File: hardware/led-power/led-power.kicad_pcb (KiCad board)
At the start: 4 copper layers, 86.4 x 86.4 mm, 104 parts, among them J1 String1, J10 PowerInput, J11 Qwiic, J12 Qwiic, J13 A0, J14 A1, J15 A2, J16 I2C Header, J17 IRQ, J2 String2, J3 String3, J4 String4, J5 String5, J6 String6, J7 String7, J8 String8, J9 PowerInput, Q1 Q_NMOS_GDS, Q2 Q_NMOS_GDS, Q3 Q_NMOS_GDS, Q4 Q_NMOS_GDS, Q5 Q_NMOS_GDS, Q6 Q_NMOS_GDS, Q7 Q_NMOS_GDS, Q8 Q_NMOS_GDS, U1 MCP6V51, U10 L78L05ACZ-AP, U11 MCP1501, U2 MCP6V51, U3 MCP6V51, U4 MCP6V51, U5 MCP6V51, U6 MCP6V51, U7 MCP6V51, U8 MCP6V51, U9 MCP23017_SO

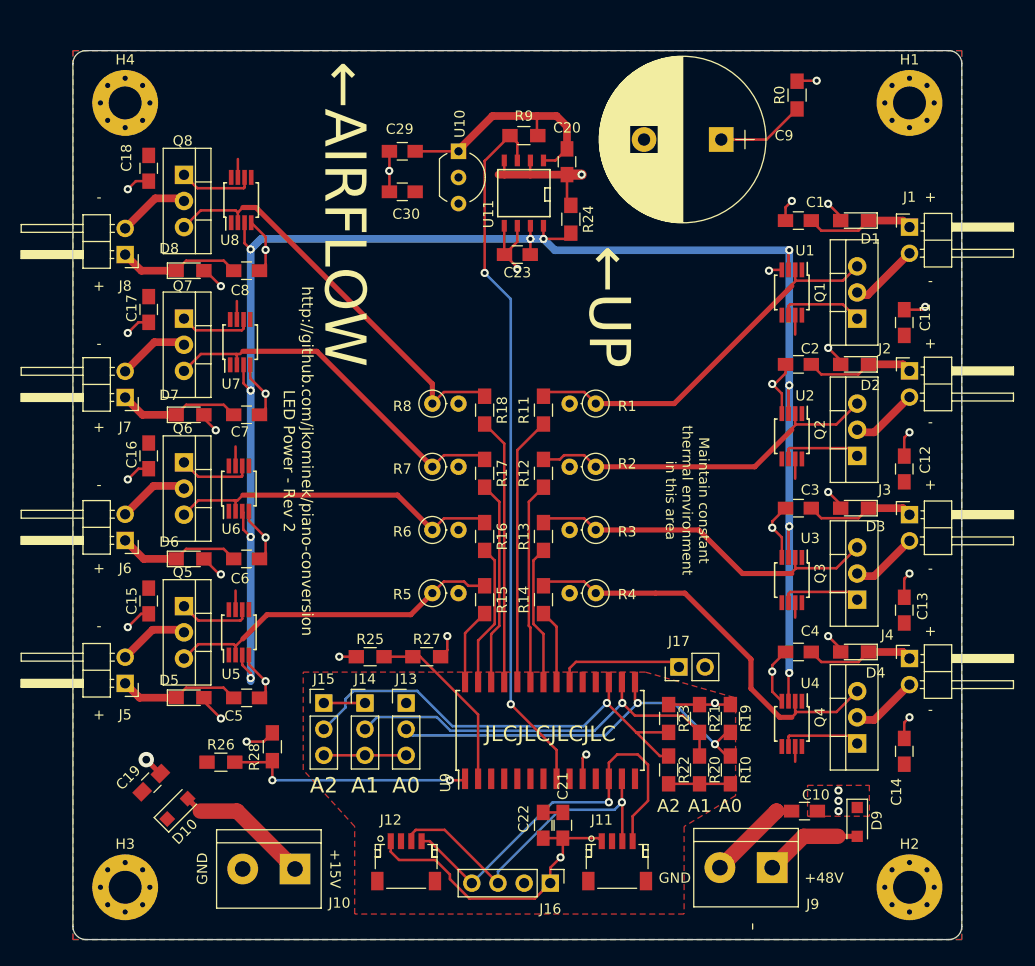
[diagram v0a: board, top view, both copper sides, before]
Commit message: LED power board improvements, per issue #42
* Increased thermal relief
* Moved C10 well away from J9
* R24 and R9 are now the same value, 3.6kohm
* Removed R0
* Removed the need for the +15V supply with an LM317.
* Removed I2C IO expander and replaced with an STM32G0
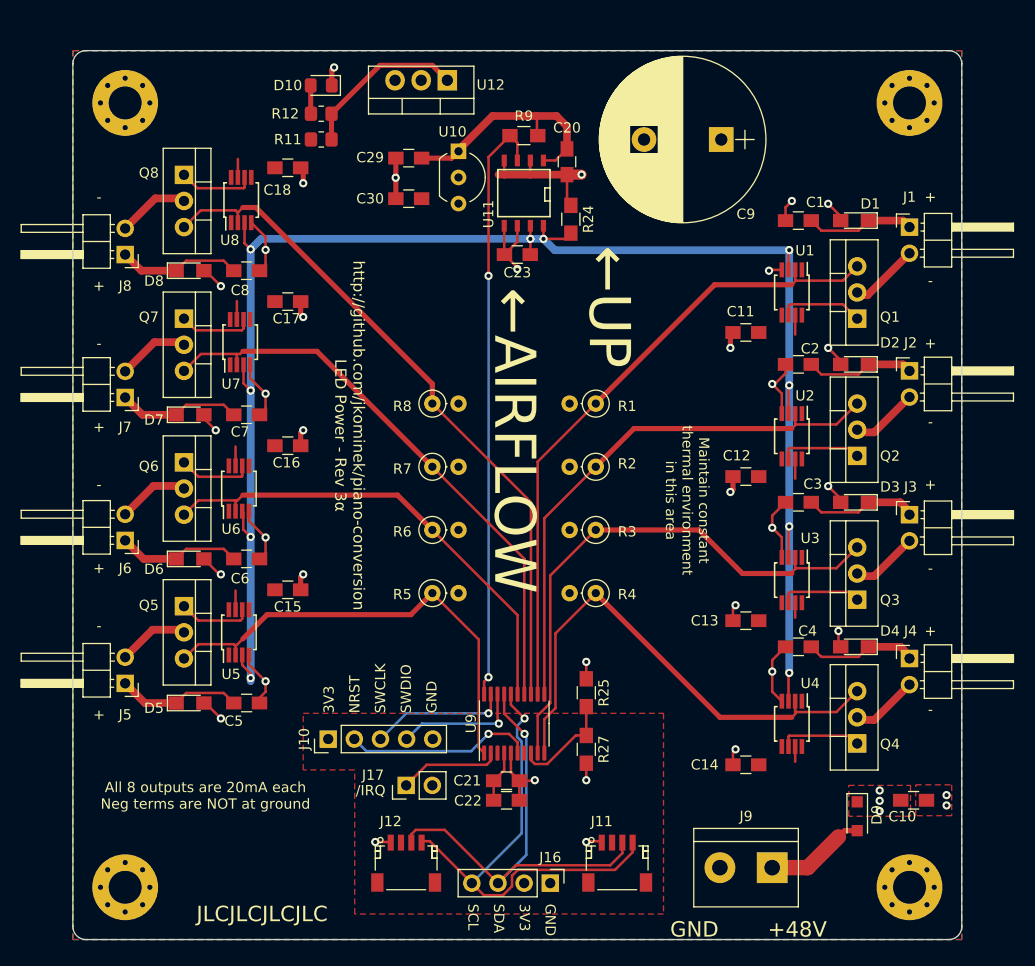
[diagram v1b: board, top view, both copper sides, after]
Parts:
- removed C19: .1uF, Capacitors_SMD:C_0805_HandSoldering
- removed J13: A0, Pin_Headers:Pin_Header_Straight_1x03_Pitch2.54mm
- removed J14: A1, Pin_Headers:Pin_Header_Straight_1x03_Pitch2.54mm
- removed J15: A2, Pin_Headers:Pin_Header_Straight_1x03_Pitch2.54mm
- removed R0: Dissipate, Resistors_SMD:R_0805_HandSoldering
- removed R10, R19, R20, R21, R22, R23: DNP, Resistors_SMD:R_0805_HandSoldering
- removed R13, R14, R15, R16, R17, R18: 43k, Resistors_SMD:R_0805_HandSoldering
- removed R26: 1300, Resistors_SMD:R_0805_HandSoldering
- removed R28: 330, Resistors_SMD:R_0805_HandSoldering
- added U12: LM317_TO-220, Package_TO_SOT_THT:TO-220-3_Vertical, F.Cu at (107.5, 74.0)
- D10: value D_Small_ALT -> 2.2Vf; footprint Diodes_SMD:D_SOD-123F -> LED_SMD:LED_0805_2012Metric_Pad1.15x1.40mm_HandSolder
- J10: value PowerInput -> Conn_01x05_Male; footprint Connectors_Terminal_Blocks:TerminalBlock_bornier-2_P5.08mm -> Connector_PinHeader_2.54mm:PinHeader_1x05_P2.54mm_Vertical
- R11: value 43k -> 1000; footprint Resistors_SMD:R_0805_HandSoldering -> Resistor_SMD:R_0805_2012Metric_Pad1.20x1.40mm_HandSolder
- R12: value 43k -> 6800; footprint Resistors_SMD:R_0805_HandSoldering -> Resistor_SMD:R_0805_2012Metric_Pad1.20x1.40mm_HandSolder
- R25: value 4700 -> 110k
- R27: value 330 -> 8.2k
- U9: value MCP23017_SO -> STM32G030Fx; footprint Housings_SOIC:SOIC-28W_7.5x17.9mm_Pitch1.27mm -> Package_SO:TSSOP-20_4.4x6.5mm_P0.65mm
- moved D10 71.7 mm to (95.2, 74.5), turned to 180 degrees
- moved R12 41.1 mm to (95.2, 77.2), turned to 180 degrees
- moved R11 34.0 mm to (95.2, 79.8), turned to 0 degrees
- moved J17 28.9 mm to (103.5, 142.5)
- moved R25 21.3 mm to (121.0, 133.5), turned to -90 degrees
- moved R27 17.9 mm to (121.0, 139.0), turned to -90 degrees
- moved C14 15.4 mm to (136.5, 140.5), turned to 180 degrees
- moved C13 15.4 mm to (136.5, 126.5), turned to 180 degrees
- moved C11 15.4 mm to (136.5, 98.5), turned to 180 degrees
- moved C12 15.4 mm to (136.5, 112.5), turned to 180 degrees
- moved C15 13.6 mm to (92.0, 123.5), turned to 0 degrees
- moved C16 13.6 mm to (92.0, 109.5), turned to 0 degrees
- moved C17 13.5 mm to (92.0, 95.5), turned to 0 degrees
- moved C18 13.5 mm to (92.0, 82.5), turned to 0 degrees
- moved J10 13.0 mm to (95.9, 138.0), turned to 90 degrees
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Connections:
- C11 pad 1: +15V -> +12V
- C12 pad 1: +15V -> +12V
- C13 pad 1: +15V -> +12V
- C14 pad 1: +15V -> +12V
- C15 pad 1: +15V -> +12V
- C16 pad 1: +15V -> +12V
- C17 pad 1: +15V -> +12V
- C18 pad 1: +15V -> +12V
- C30 pad 1: +15V -> +12V
- D10 pad 1: +15V -> GND
- J10 pad 1: Net-(D10-Pad2) -> +3V3
- J10 pad 2: GND -> /NRST
- J17 pad 1: /~IRQ -> /~{IRQ}
- R11 pad 1: /Feedback1 -> +12V
- R12 pad 1: /Feedback2 -> Net-(R11-Pad2)
- R12 pad 2: Net-(R12-Pad2) -> Net-(D10-Pad2)
- R9 pad 2: /~SHDN -> /~{SHDN}
- U1 pad 1: (no net) -> unconnected-(U1-Pad1)
- U1 pad 5: (no net) -> unconnected-(U1-Pad5)
- U1 pad 7: +15V -> +12V
- U1 pad 8: (no net) -> unconnected-(U1-Pad8)
- U10 pad 3: +15V -> +12V
- U11 pad 3: /~SHDN -> /~{SHDN}
- U2 pad 1: (no net) -> unconnected-(U2-Pad1)
- U2 pad 5: (no net) -> unconnected-(U2-Pad5)
- U2 pad 7: +15V -> +12V
- U2 pad 8: (no net) -> unconnected-(U2-Pad8)
- U3 pad 1: (no net) -> unconnected-(U3-Pad1)
- U3 pad 5: (no net) -> unconnected-(U3-Pad5)
- U3 pad 7: +15V -> +12V
- U3 pad 8: (no net) -> unconnected-(U3-Pad8)
- U4 pad 1: (no net) -> unconnected-(U4-Pad1)
- U4 pad 5: (no net) -> unconnected-(U4-Pad5)
- U4 pad 7: +15V -> +12V
- U4 pad 8: (no net) -> unconnected-(U4-Pad8)
- U5 pad 1: (no net) -> unconnected-(U5-Pad1)
- U5 pad 5: (no net) -> unconnected-(U5-Pad5)
- U5 pad 7: +15V -> +12V
- U5 pad 8: (no net) -> unconnected-(U5-Pad8)
- U6 pad 1: (no net) -> unconnected-(U6-Pad1)
- U6 pad 5: (no net) -> unconnected-(U6-Pad5)
- U6 pad 7: +15V -> +12V
- U6 pad 8: (no net) -> unconnected-(U6-Pad8)
- U7 pad 1: (no net) -> unconnected-(U7-Pad1)
- U7 pad 5: (no net) -> unconnected-(U7-Pad5)
- U7 pad 7: +15V -> +12V
- U7 pad 8: (no net) -> unconnected-(U7-Pad8)
- U8 pad 1: (no net) -> unconnected-(U8-Pad1)
- U8 pad 5: (no net) -> unconnected-(U8-Pad5)
- U8 pad 7: +15V -> +12V
- U8 pad 8: (no net) -> unconnected-(U8-Pad8)
- U9 pad 1: /15V_SENSE -> /Feedback5
- U9 pad 10: GND -> /Feedback4
- U9 pad 11: (no net) -> /Feedback2
- U9 pad 12: /SCL -> /Feedback1
- U9 pad 13: /SDA -> /Feedback8
- U9 pad 14: (no net) -> /Feedback7
- U9 pad 15: /A0 -> /Feedback6
- U9 pad 16: /A1 -> /SCL
- U9 pad 17: /A2 -> /SDA
- U9 pad 18: +3V3 -> /SWDIO
- U9 pad 19: (no net) -> /SWCLK
- U9 pad 2: /48V_SENSE -> /~{IRQ}
- U9 pad 20: /~IRQ -> /~{SHDN}
- U9 pad 3: (no net) -> unconnected-(U9-Pad3)
- U9 pad 4: (no net) -> +3V3
- U9 pad 5: (no net) -> GND
- U9 pad 6: (no net) -> /NRST
- U9 pad 7: (no net) -> unconnected-(U9-Pad7)
- U9 pad 8: /~SHDN -> /48V_SENSE
- U9 pad 9: +3V3 -> /Feedback3
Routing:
- net /~SHDN: track 69.1 -> 0.00 mm, vias 2 -> 0
- net /~{SHDN}: track 0.00 -> 58.0 mm, vias 0 -> 2
- net GND: track 148.6 -> 95.4 mm
- net /A2: track 45.3 -> 0.00 mm, vias 1 -> 0
- net /A1: track 40.2 -> 0.00 mm, vias 1 -> 0
- net /A0: track 39.9 -> 0.00 mm, vias 2 -> 0
- net /Feedback8: track 41.1 -> 67.5 mm
- net Net-(R18-Pad2): track 25.9 -> 0.00 mm
- net /Feedback1: track 37.8 -> 62.6 mm
- net /15V_SENSE: track 24.4 -> 0.00 mm, vias 2 -> 0
- net /Feedback7: track 36.4 -> 56.4 mm
- net Net-(R17-Pad2): track 19.8 -> 0.00 mm
- net Net-(R12-Pad2): track 19.6 -> 0.00 mm
- net /NRST: track 0.00 -> 18.4 mm, vias 0 -> 1
- net /Feedback2: track 34.8 -> 53.2 mm
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- added copper zone on F.Cu, net +12V
- added copper zone on F.Cu, net GND
- removed copper zone on F.Cu, net +15V
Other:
- net class Default removed
- board text added: "/IRQ"
- board text added: "3V3"
- board text added: "All 8 outputs are 20mA each Neg terms are NOT at ground"
- board text added: "NRST"
- board text added: "SCL"
- board text added: "SDA"
- board text added: "SWCLK"
- board text added: "SWDIO"
- board text added: "http://github.com/jkominek/piano-conversion LED Power - Rev 3α"
- board text removed: "+15V"
- board text removed: "A0"
- board text removed: "A1"
- board text removed: "A2"
- board text removed: "http://github.com/jkominek/piano-conversion LED Power - Rev 2"

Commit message: Use a BJT to pull down the /IRQ line.
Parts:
- added Q9: Q_NPN_BEC, Package_TO_SOT_SMD:SOT-23, F.Cu at (105.5, 142.5)
- added R10: 10k, Resistor_SMD:R_0805_2012Metric_Pad1.20x1.40mm_HandSolder, F.Cu at (109.0, 142.5)
- C1, C10, C11, C12, C13, C14, C15, C16, C17, C18, C2, C20, C21, C22, C23, C29, C3, C30, C4, C5, C6, C7, C8: footprint Capacitors_SMD:C_0805_HandSoldering -> Capacitor_SMD:C_0805_2012Metric_Pad1.18x1.45mm_HandSolder
- D1, D2, D3, D4, D5, D6, D7, D8: footprint LEDs:LED_0805_HandSoldering -> LED_SMD:LED_0805_2012Metric_Pad1.15x1.40mm_HandSolder
- R24, R25, R9: footprint Resistors_SMD:R_0805_HandSoldering -> Resistor_SMD:R_0805_2012Metric_Pad1.20x1.40mm_HandSolder
- R27: value 8.2k -> 4.7k; footprint Resistors_SMD:R_0805_HandSoldering -> Resistor_SMD:R_0805_2012Metric_Pad1.20x1.40mm_HandSolder
- moved J17 5.00 mm to (98.5, 142.5)
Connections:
- J17 pad 1: /~{IRQ} -> Net-(J17-Pad1)
- U9 pad 2: /~{IRQ} -> /IRQ
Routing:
- net /~{IRQ}: track 9.96 -> 0.00 mm
- net Net-(J17-Pad1): track 0.00 -> 8.60 mm
- net /IRQ: track 0.00 -> 4.14 mm
- net GND: track 95.4 -> 99.3 mm
- net Net-(Q9-Pad1): track 0.00 -> 3.35 mm
